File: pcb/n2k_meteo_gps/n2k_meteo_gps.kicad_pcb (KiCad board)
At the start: 2 copper layers, 58.4 x 69.8 mm, 21 parts, among them J1 I2C, J2 1W_DHT22, J4 I2C_BME280, J6 GPS, J7 I2C, J8 CAN Term, J9 N2K, U1 ESP32-DevKitC, U2 TSR_1-2450, U3 MCP2562-E-P

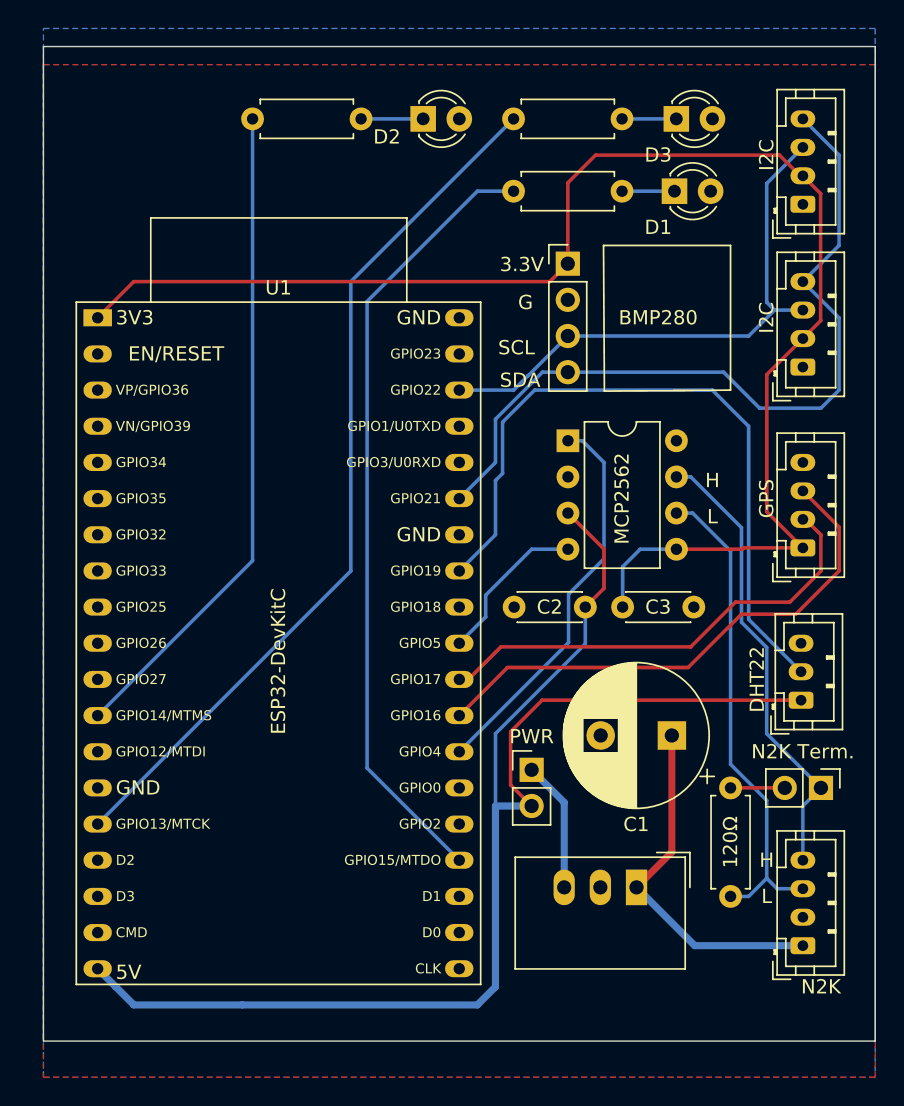
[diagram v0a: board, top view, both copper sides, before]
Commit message: New version with BLE setup instead of web
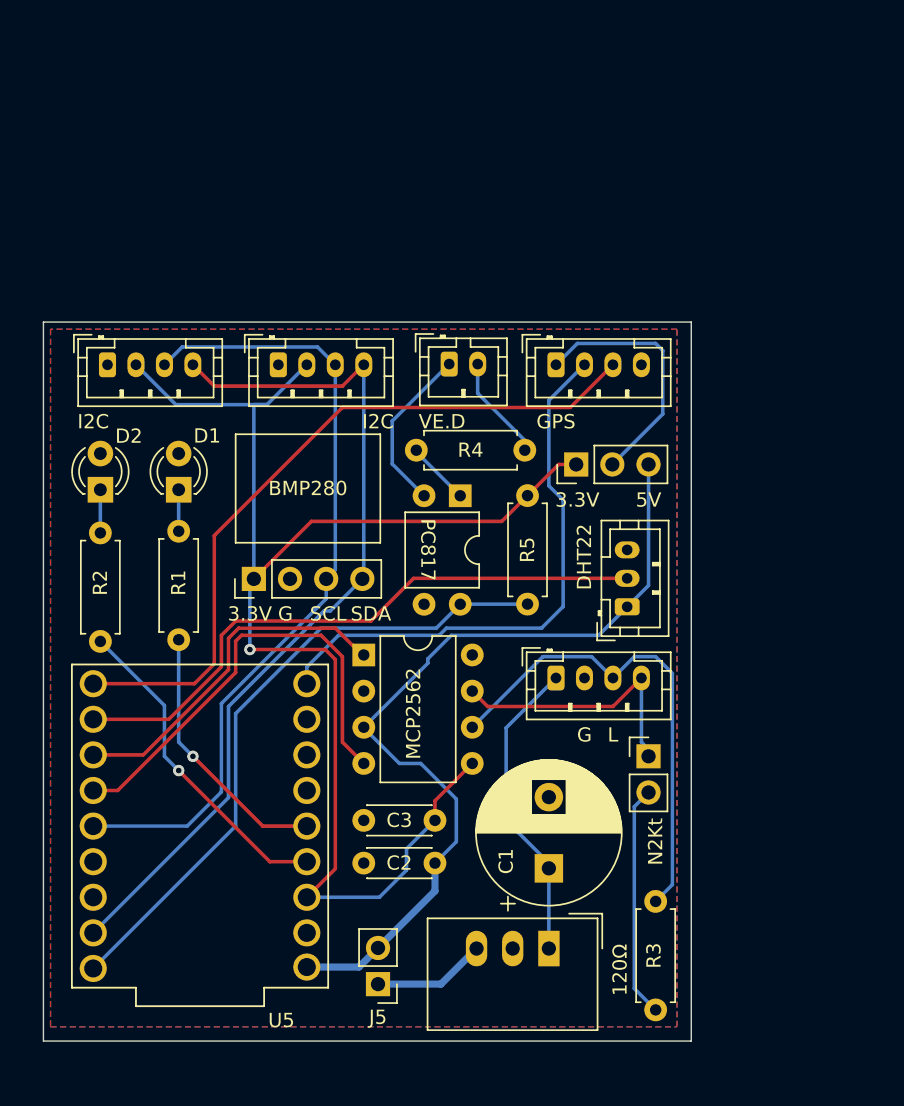
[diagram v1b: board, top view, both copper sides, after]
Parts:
- removed D3: LED, LED_THT:LED_D3.0mm
- removed U1: ESP32-DevKitC, PCM_Espressif:ESP32-DevKitC
- added J10: 3.3-5V, Connector_PinHeader_2.54mm:PinHeader_1x03_P2.54mm_Vertical, F.Cu at (56.5, 54.8)
- added J3: VE.Direct, Connector_JST:JST_PH_B2B-PH-K_1x02_P2.00mm_Vertical, F.Cu at (47.5, 47.7)
- added R5: 4.7KΩ, Resistor_THT:R_Axial_DIN0207_L6.3mm_D2.5mm_P7.62mm_Horizontal, F.Cu at (53.0, 56.9)
- added U4: PC817, Package_DIP:DIP-4_W7.62mm, F.Cu at (48.3, 57.0)
- added U5: ESP32-C3_SUPERMINI, esp32_c3_supermini:WAVESHARE_DEVKIT_ESP32-C3-ZERO, F.Cu at (30.1, 80.2)
- R1: value 100 -> 100Ω
- R2: value 120 -> 100Ω
- R3: value 100 -> 120Ω
- R4: value 100 -> 180Ω
- moved R3 58.7 mm to (62.0, 85.4), turned to -90 degrees
- moved R2 51.1 mm to (23.1, 59.6), turned to -90 degrees
- moved J1 48.8 mm to (23.6, 47.8), turned to 0 degrees
- moved D1 40.6 mm to (28.6, 56.5), turned to 90 degrees
- moved R1 39.2 mm to (28.6, 59.4), turned to -90 degrees
- moved J7 38.5 mm to (35.5, 47.8), turned to 0 degrees
- moved D2 34.5 mm to (23.1, 56.5), turned to 90 degrees
- moved J4 31.2 mm to (33.8, 62.8), turned to 90 degrees
- moved R4 27.4 mm to (45.2, 53.8), turned to 0 degrees
- moved J9 25.6 mm to (55.0, 69.8), turned to 0 degrees
- moved J6 21.6 mm to (55.0, 47.8), turned to 0 degrees
- moved C2 20.9 mm to (46.5, 82.8)
- moved U3 20.8 mm to (41.5, 68.1)
- moved C3 20.0 mm to (46.5, 79.8), turned to 180 degrees
- moved J5 18.5 mm to (42.5, 91.2), turned to 180 degrees
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- renumbered PWR to J5
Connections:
- net Net-(J2-Pin_1) renamed +5V
- C3 pad 1: Net-(J1-Pin_2) -> +3.3V
- J1 pad 2: Net-(J1-Pin_2) -> +3.3V
- J4 pad 1: Net-(J1-Pin_2) -> +3.3V
- J6 pad 1: Net-(J1-Pin_2) -> Net-(J10-Pin_2)
- J7 pad 2: Net-(J1-Pin_2) -> +3.3V
- R2 pad 1: Net-(J9-Pin_3) -> Net-(D2-K)
- R2 pad 2: Net-(J8-Pin_2) -> Net-(U5-GPIO0)
- R3 pad 1: Net-(D2-K) -> Net-(J9-Pin_3)
- R3 pad 2: Net-(U1-MTMS/GPIO14/ADC2_CH6) -> Net-(J8-Pin_2)
- U3 pad 5: Net-(J1-Pin_2) -> +3.3V
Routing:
- net Net-(J1-Pin_2): track 103.5 -> 0.00 mm
- net +3.3V: track 0.00 -> 99.5 mm, vias 0 -> 1
- net Net-(J3-Pin_2): track 61.6 -> 7.42 mm
- net Net-(U1-MTMS/GPIO14/ADC2_CH6): track 46.4 -> 0.00 mm
- net Net-(U5-GPIO21): track 0.00 -> 45.7 mm
- net +5V: track 96.7 -> 59.7 mm
- net Net-(U5-GPIO1): track 55.4 -> 18.6 mm, vias 0 -> 1
- net Net-(U5-GPIO0): track 0.00 -> 23.0 mm, vias 0 -> 1
- net Net-(U3-RXD): track 11.3 -> 32.1 mm
- net Net-(J10-Pin_2): track 0.00 -> 17.8 mm
- net Net-(J1-Pin_3): track 39.2 -> 56.3 mm
- net Net-(J6-Pin_3): track 37.6 -> 51.1 mm
- net Net-(J8-Pin_1): track 32.2 -> 18.9 mm
- net Net-(J8-Pin_2): track 3.81 -> 16.3 mm
- net Net-(J3-Pin_1): track 0.00 -> 11.8 mm
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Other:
- board size 58.4 x 69.8 mm -> 45.5 x 50.5 mm
- board text added: "5V"
- board text added: "N2Kt"
- board text added: "PC817"
- board text added: "VE.D"
- board text removed: "H"
- board text removed: "N2K"
- board text removed: "N2K Term."

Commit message: pcb
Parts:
- removed J1, J7: I2C, Connector_JST:JST_PH_B4B-PH-K_1x04_P2.00mm_Vertical
- removed J2: 1W_DHT22, Connector_JST:JST_PH_B3B-PH-K_1x03_P2.00mm_Vertical
- removed J3: VE.Direct, Connector_JST:JST_PH_B2B-PH-K_1x02_P2.00mm_Vertical
- removed J4: I2C_BME280, Connector_PinHeader_2.54mm:PinHeader_1x04_P2.54mm_Vertical
- removed J5: 5V switch, Connector_PinHeader_2.54mm:PinHeader_1x02_P2.54mm_Vertical
- removed J6: GPS, Connector_JST:JST_PH_B4B-PH-K_1x04_P2.00mm_Vertical
- removed J8: CAN Term, Connector_PinHeader_2.54mm:PinHeader_1x02_P2.54mm_Vertical
- removed J9: N2K, Connector_JST:JST_PH_B4B-PH-K_1x04_P2.00mm_Vertical
- removed U2: TSR_1-2450, Converter_DCDC:Converter_DCDC_TRACO_TSR-1_THT
- added C4: 10nanoF, Capacitor_THT:C_Disc_D7.0mm_W2.5mm_P5.00mm, F.Cu at (33.5, 78.2)
- added D3: 1N4001, Diode_THT:D_DO-41_SOD81_P10.16mm_Horizontal, F.Cu at (33.5, 81.8)
- added J_BMP1: I2C_BME280, Connector_PinHeader_2.54mm:PinHeader_1x04_P2.54mm_Vertical, F.Cu at (57.3, 58.8)
- added J_CAN1: CAN Term, Connector_PinHeader_2.54mm:PinHeader_1x02_P2.54mm_Vertical, F.Cu at (69.0, 73.2)
- added J_DHT1: 1W_DHT22, Connector_JST:JST_PH_B4B-PH-K_1x04_P2.00mm_Vertical, F.Cu at (58.0, 64.8)
- added J_GND1: CAN GND, MountingHole:MountingHole_2.2mm_M2_DIN965_Pad_TopBottom, F.Cu at (70.5, 91.8)
- added J_H1: CAN H, MountingHole:MountingHole_2.2mm_M2_DIN965_Pad_TopBottom, F.Cu at (70.5, 84.8)
- added J_I2C1: I2C, Connector_JST:JST_PH_B4B-PH-K_1x04_P2.00mm_Vertical, F.Cu at (58.0, 46.8)
- added J_L1: CAN L, MountingHole:MountingHole_2.2mm_M2_DIN965_Pad_TopBottom, F.Cu at (64.0, 84.8)
- added J_PWR1: 5V switch, Connector_PinHeader_2.54mm:PinHeader_1x02_P2.54mm_Vertical, F.Cu at (41.3, 86.2)
- added J_UART1: GPS, Connector_JST:JST_PH_B4B-PH-K_1x04_P2.00mm_Vertical, F.Cu at (70.0, 67.2)
- added J_VCC1: CAN 12V, MountingHole:MountingHole_2.2mm_M2_DIN965_Pad_TopBottom, F.Cu at (64.0, 91.8)
- added J_VE1: VE.Direct, Connector_JST:JST_PH_B2B-PH-K_1x02_P2.00mm_Vertical, F.Cu at (23.1, 58.2)
- added J_W1: Engine RPM Input, TerminalBlock_Phoenix:TerminalBlock_Phoenix_MKDS-1,5-2_1x02_P5.00mm_Horizontal, F.Cu at (22.6, 89.1)
- added R10: 10K, Resistor_THT:R_Axial_DIN0207_L6.3mm_D2.5mm_P7.62mm_Horizontal, F.Cu at (37.5, 72.9)
- added R11: 4.7K, Resistor_THT:R_Axial_DIN0207_L6.3mm_D2.5mm_P7.62mm_Horizontal, F.Cu at (21.7, 73.2)
- added R8: 4.7K, Resistor_THT:R_Axial_DIN0207_L6.3mm_D2.5mm_P7.62mm_Horizontal, F.Cu at (42.5, 72.8)
- added U1: LM7805_TO220, Package_TO_SOT_THT:TO-220-3_Vertical, F.Cu at (46.6, 90.8)
- added U6: PC817, Package_DIP:DIP-4_W7.62mm, F.Cu at (21.6, 78.0)
- C1: value C_470microF -> 100uF
- C2, C3: value 10nanoF -> 100nF
- U5: footprint esp32_c3_supermini:WAVESHARE_DEVKIT_ESP32-C3-ZERO -> Library:WAVESHARE_DEVKIT_ESP32-C3-ZERO
- moved U5 28.5 mm to (45.5, 56.2), turned to 0 degrees
- moved U4 28.1 mm to (21.8, 66.0), turned to 0 degrees
- moved R5 23.6 mm to (29.6, 54.4)
- moved R2 19.2 mm to (33.5, 43.4)
- moved R4 19.0 mm to (34.0, 69.1), turned to 90 degrees
- moved U3 18.9 mm to (59.9, 72.8), turned to -90 degrees
- moved R1 16.0 mm to (27.6, 43.4)
- moved J10 15.3 mm to (71.0, 50.2), turned to 0 degrees
- moved D1 13.8 mm to (21.3, 44.8), turned to 0 degrees
- moved C2 11.1 mm to (48.0, 71.8), turned to -90 degrees
- moved C1 8.06 mm to (55.5, 91.1)
- moved R3 7.14 mm to (64.5, 78.8), turned to 0 degrees
- moved D2 6.11 mm to (21.1, 50.8), turned to 0 degrees
- moved C3 1.58 mm to (48.0, 79.2), turned to -90 degrees
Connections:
- R5 pad 2: Net-(U5-GPIO21) -> Net-(U5-GPIO5)
- U4 pad 4: Net-(U5-GPIO21) -> Net-(U5-GPIO5)
- U5 pad 2: unconnected-(U5-GPIO2-Pad2) -> Net-(J_UART1-Pin_4)
- U5 pad 20: Net-(J1-Pin_4) -> unconnected-(U5-GPIO20-Pad20)
- U5 pad 21: Net-(U5-GPIO21) -> unconnected-(U5-GPIO21-Pad21)
- U5 pad 3: unconnected-(U5-GPIO3-Pad3) -> Net-(J_UART1-Pin_3)
- U5 pad 4: unconnected-(U5-GPIO4-Pad4) -> Net-(U5-GPIO4)
- U5 pad 5: Net-(J6-Pin_2) -> Net-(U5-GPIO5)
- U5 pad 7: Net-(J2-Pin_2) -> Net-(U3-TXD)
- U5 pad 8: Net-(U3-TXD) -> Net-(U3-RXD)
- U5 pad 9: Net-(U3-RXD) -> Net-(J_BMP1-Pin_4)
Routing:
- net Net-(J1-Pin_4): track 61.3 -> 0.00 mm
- net Net-(U5-GPIO21): track 45.7 -> 0.00 mm
- net Net-(J2-Pin_2): track 42.9 -> 0.00 mm
- net Net-(J_DHT1-Pin_2): track 51.1 -> 8.86 mm
- net Net-(J_UART1-Pin_4): track 0.00 -> 40.0 mm
- net Net-(J6-Pin_2): track 39.4 -> 0.00 mm
- net Net-(J_UART1-Pin_3): track 0.00 -> 38.6 mm
- net Net-(U5-GPIO4): track 0.00 -> 38.4 mm
- net +5V: track 59.7 -> 94.7 mm
- net Net-(J_W1-Pin_1): track 0.00 -> 34.8 mm
- net Net-(J_BMP1-Pin_4): track 0.00 -> 33.4 mm
- net Net-(J_BMP1-Pin_3): track 56.3 -> 25.1 mm
- net Net-(R10-Pad1): track 0.00 -> 22.1 mm
- net Net-(U3-RXD): track 32.1 -> 13.6 mm
- net Net-(U5-GPIO0): track 23.0 -> 5.61 mm, vias 1 -> 0
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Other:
- board size 45.5 x 50.5 mm -> 55 x 54.5 mm
- board text added: "AB"
- board text removed: "120Ω"
- board text removed: "3.3V"
- board text removed: "5V"
- board text removed: "BMP280"
- board text removed: "DHT22"
- board text removed: "G"
- board text removed: "GPS"
- board text removed: "I2C"
- board text removed: "L"
- board text removed: "MCP2562"
- board text removed: "N2Kt"
- board text removed: "PC817"
- board text removed: "SCL"
- board text removed: "SDA"
- board text removed: "VE.D"

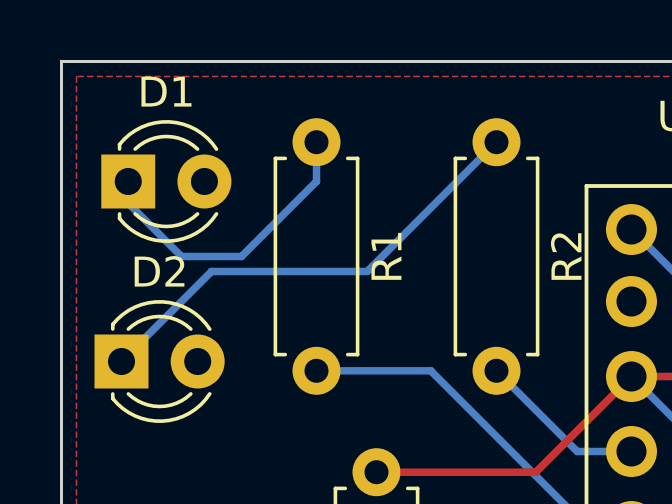
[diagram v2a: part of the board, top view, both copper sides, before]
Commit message: -Fixed but to prevent N2K to be initialized with 0xFF source -Made GPS UART speed static (def 9600) -Reset n2k stats every 10s (instead of accumulated figures, get the last period only) - added unix_time to UART GPS
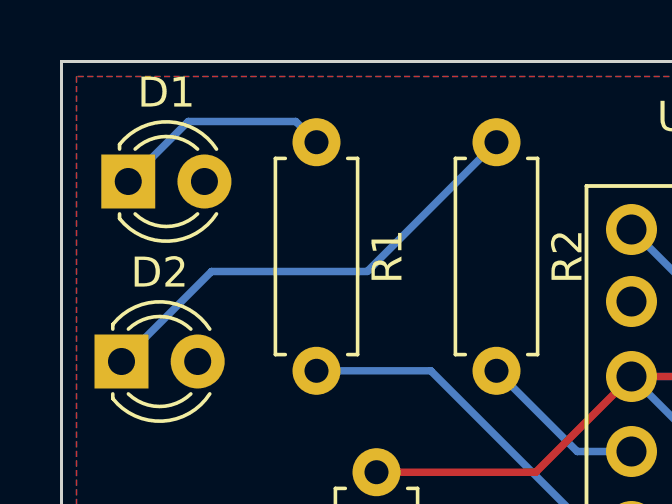
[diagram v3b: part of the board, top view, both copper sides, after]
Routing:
- net Net-(D1-K): track 10.1 -> 7.39 mm
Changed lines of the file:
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@@
 	)
 	(segment
-		(start 27.55 44.75)
+		(start 23.275 42.75)
+		(end 26.86 42.75)
+		(width 0.25)
+		(layer "B.Cu")
+		(net 2)
+	)
+	(segment
+		(start 26.86 42.75)
 		(end 27.55 43.44)
 		(width 0.25)
@@
 	)
 	(segment
-		(start 21.275 45.475)
-		(end 23.05 47.25)
+		(start 21.275 44.75)
+		(end 23.275 42.75)
 		(width 0.25)
 		(layer "B.Cu")
-		(net 2)
-	)
-	(segment
-		(start 23.05 47.25)
-		(end 25.05 47.25)
-		(width 0.25)
-		(layer "B.Cu")
-		(net 2)
-	)
-	(segment
-		(start 21.275 44.75)
-		(end 21.275 45.475)
-		(width 0.25)
-		(layer "B.Cu")
-		(net 2)
-	)
-	(segment
-		(start 25.05 47.25)
-		(end 27.55 44.75)
-		(width 0.25)
-		(layer "B.Cu")
